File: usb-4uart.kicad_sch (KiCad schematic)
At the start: 49 parts, among them J1 Conn_02x05_Odd_Even, X1 24MHz

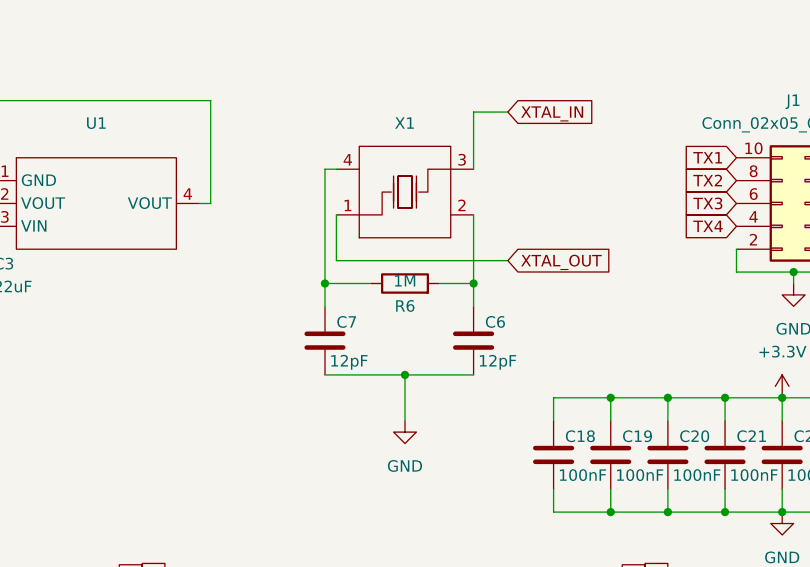
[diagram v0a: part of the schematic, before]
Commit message: -updated layout and traces -relocated caps -rotated devices -usb paths more even now
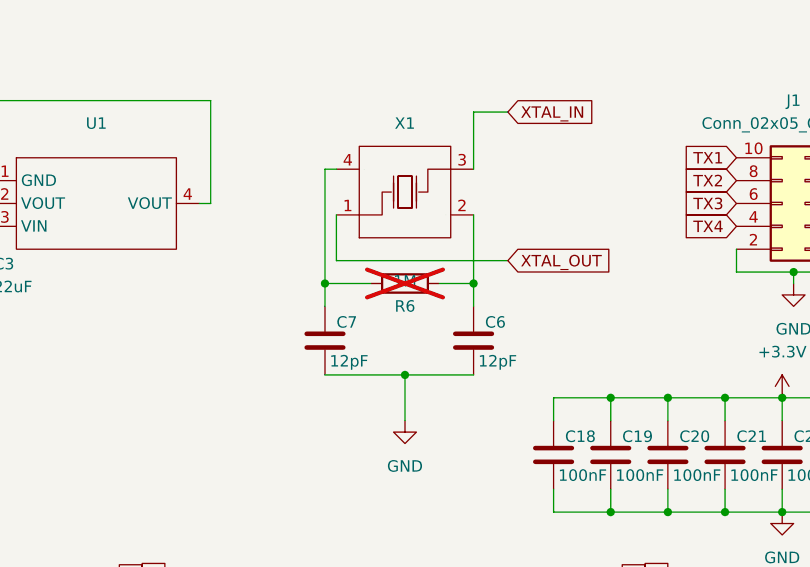
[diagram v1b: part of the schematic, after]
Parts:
- R6: now not fitted

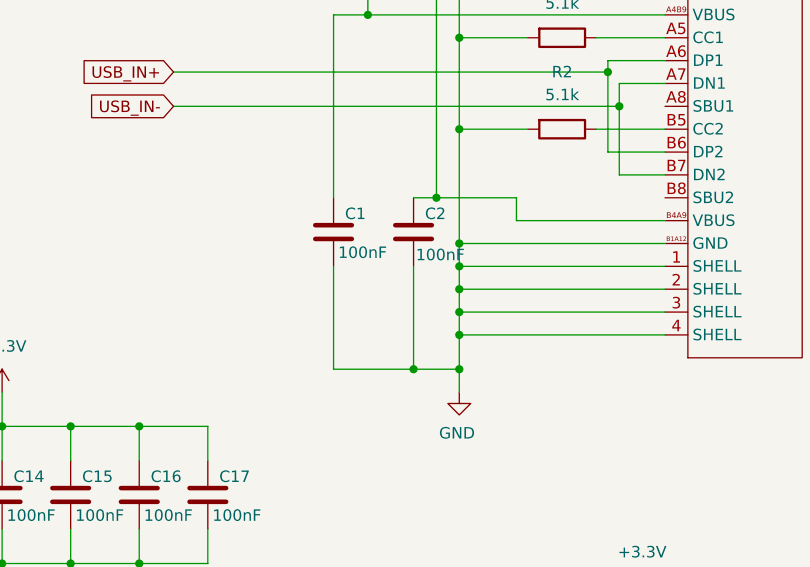
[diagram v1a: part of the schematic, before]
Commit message: updated cp2102 vias updated crystal circuitry updated 3v3 joints
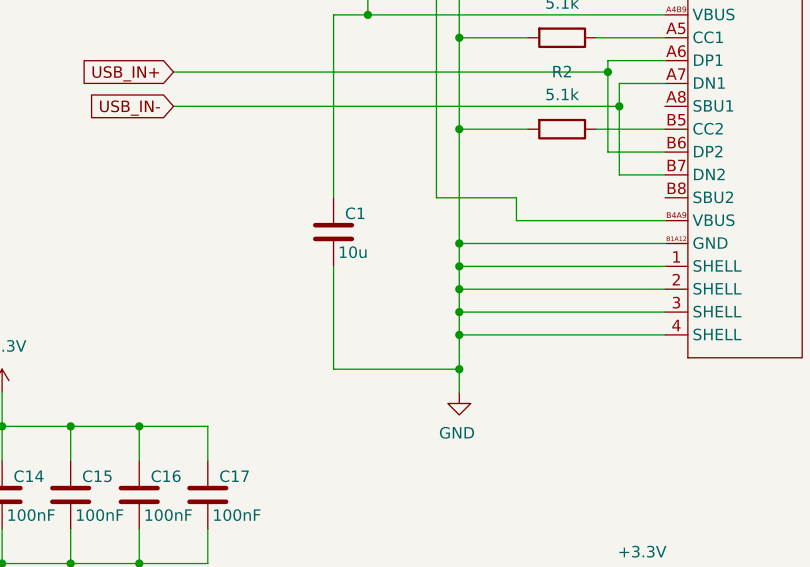
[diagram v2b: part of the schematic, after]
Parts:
- removed C2: 100nF, Capacitor_SMD:C_0201_0603Metric, symbol Device:C
- C1: value 100nF -> 10u
- C3: footprint Capacitor_Tantalum_SMD:CP_EIA-1608-08_AVX-J -> Capacitor_Tantalum_SMD:CP_EIA-3216-18_Kemet-A

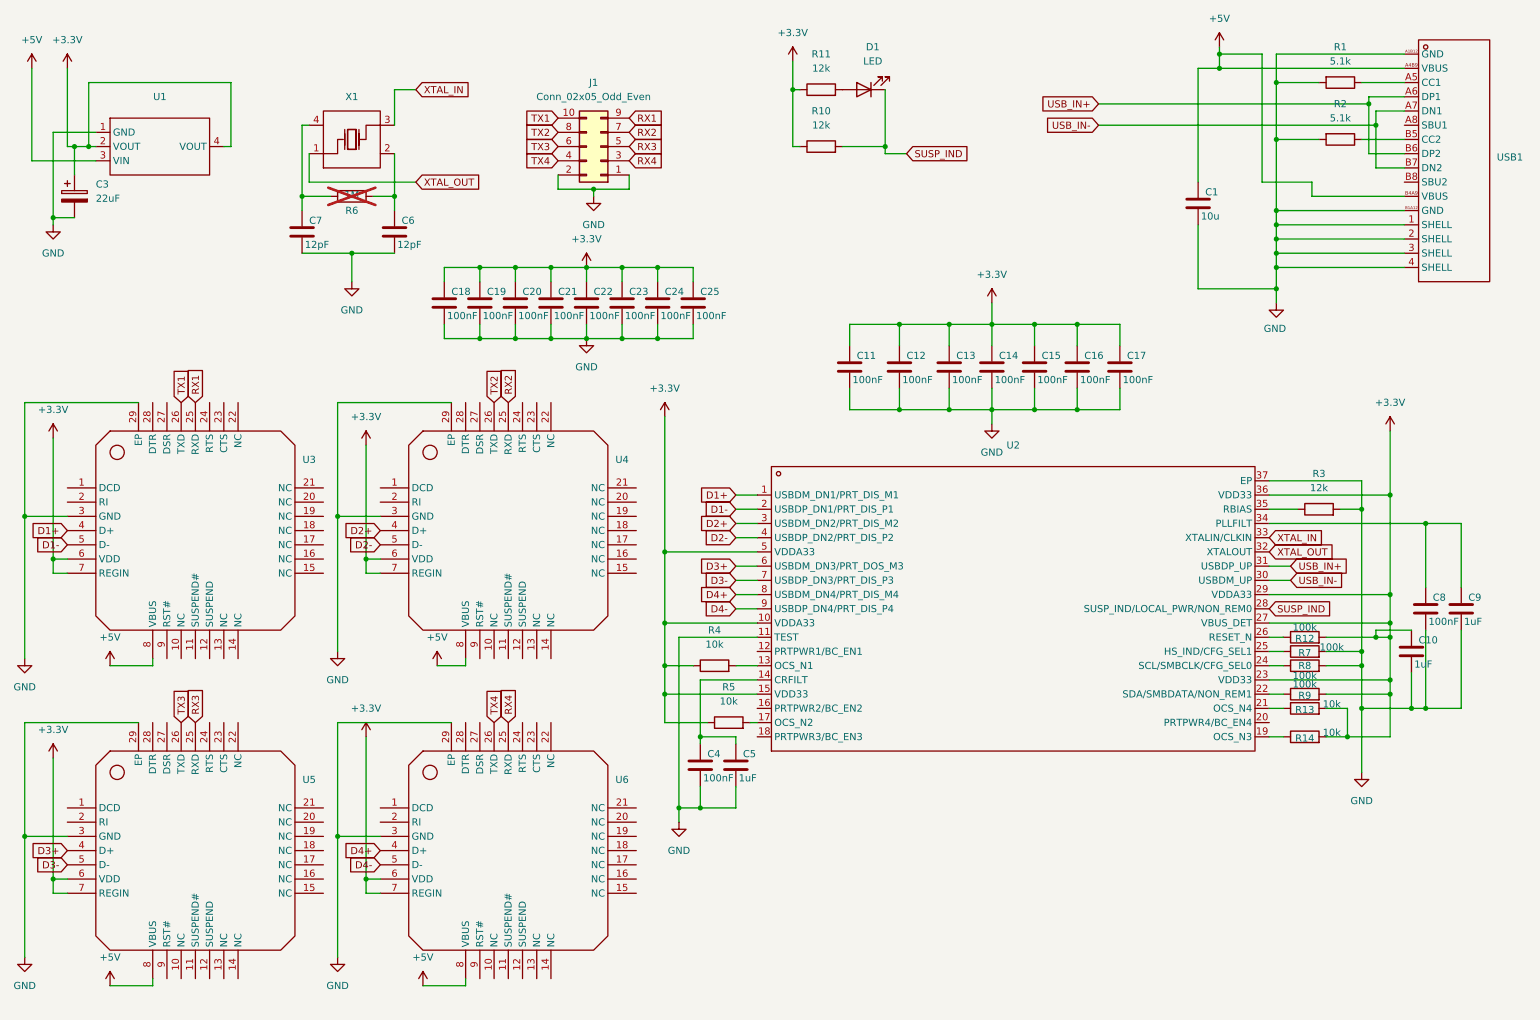
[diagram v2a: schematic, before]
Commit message: -updated to kicad 9.0.1 -reworked layout with correct footprints
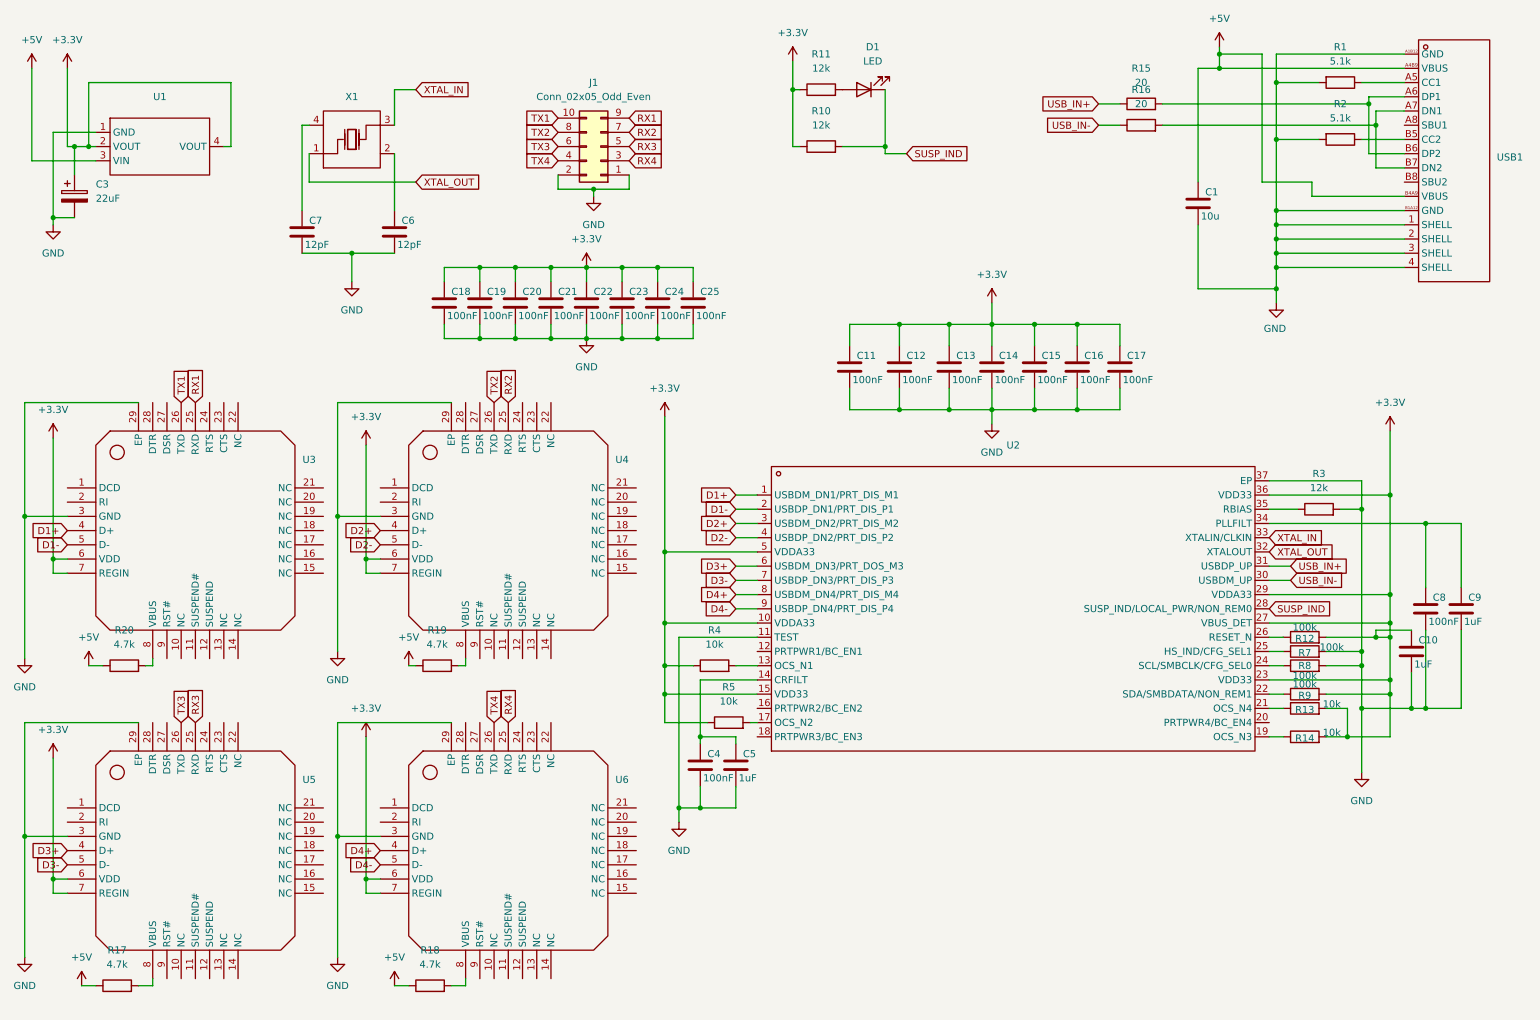
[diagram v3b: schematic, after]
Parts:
- removed R6: 1M, Resistor_SMD:R_0201_0603Metric, symbol Device:R
- added R15, R16: 20, Resistor_SMD:R_0402_1005Metric, symbol Device:R
- added R17, R18, R19, R20: 4.7k, Resistor_SMD:R_0402_1005Metric, symbol Device:R
- C10, C11, C12, C13, C14, C15, C16, C17, C18, C19, C20, C21, C22, C23, C24, C25, C4, C5, C6, C7, C8, C9: footprint Capacitor_SMD:C_0201_0603Metric -> Capacitor_SMD:C_0402_1005Metric
- R1, R10, R11, R12, R13, R14, R2, R3, R4, R5, R7, R8, R9: footprint Resistor_SMD:R_0201_0603Metric -> Resistor_SMD:R_0402_1005Metric
- U1: LCSC (none) -> C6186
- U2: LCSC (none) -> C16251
- U3, U4, U5, U6: LCSC (none) -> C6568
- USB1: LCSC (none) -> C393939
- X1: LCSC (none) -> C70590
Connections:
- net +5V: now also R17.1, R18.1, R19.1, R20.1; no longer U3.8 (VBUS), U4.8 (VBUS), U5.8 (VBUS), U6.8 (VBUS)
- net USB_IN+: now also R15.1; no longer USB1.A6 (DP1), USB1.B6 (DP2)
- net USB_IN-: now also R16.1; no longer USB1.A7 (DN1), USB1.B7 (DN2)
- new net: R15.2, USB1.A6 (DP1), USB1.B6 (DP2)
- new net: R16.2, USB1.A7 (DN1), USB1.B7 (DN2)
- new net: R19.2, U4.8 (VBUS)
- new net: R18.2, U6.8 (VBUS)
- new net: R20.2, U3.8 (VBUS)
- new net: R17.2, U5.8 (VBUS)
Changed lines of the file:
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@@
 (kicad_sch
-	(version 20231120)
+	(version 20250114)
 	(generator "eeschema")
-	(generator_version "8.0")
+	(generator_version "9.0")
 	(paper "A4")

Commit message: updated bom and clock
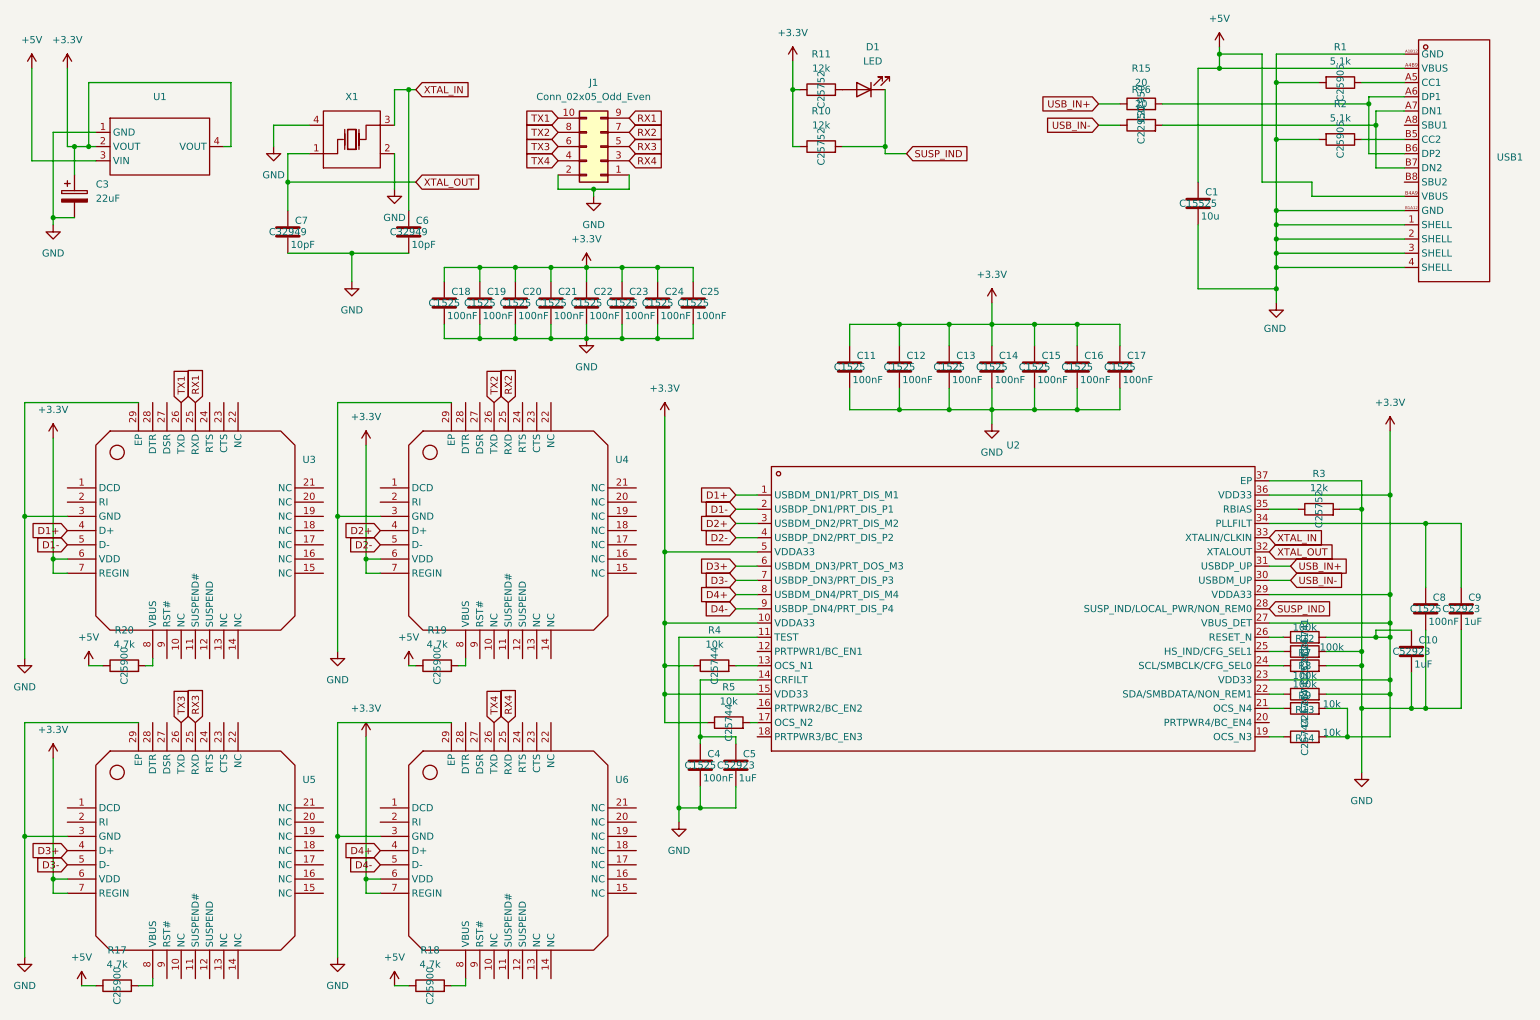
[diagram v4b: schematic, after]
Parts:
- C1: footprint Capacitor_SMD:C_0201_0603Metric -> Capacitor_SMD:C_0603_1608Metric; LCSC (none) -> C15525
- C10, C5, C9: LCSC (none) -> C52923
- C11, C12, C13, C14, C15, C16, C17, C18, C19, C20, C21, C22, C23, C24, C25, C4, C8: LCSC (none) -> C1525
- C6, C7: value 12pF -> 10pF; LCSC (none) -> C32949
- J1: LCSC C60563 -> C60563
- R1, R2: LCSC (none) -> C25905
- R10, R11, R3: LCSC (none) -> C25752
- R12, R7, R8, R9: LCSC (none) -> C25741
- R13, R14, R4, R5: LCSC (none) -> C25744
- R15, R16: footprint Resistor_SMD:R_0402_1005Metric -> Resistor_SMD:R_0603_1608Metric; LCSC (none) -> C22950
- R17, R18, R19, R20: LCSC (none) -> C25900
- X1: LCSC C70590 -> C70583; Supplier Part C70590 -> C70583
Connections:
- net GND: now also X1.2 (GND), X1.4 (GND)
- net XTAL_IN: now also C6.1
- net XTAL_OUT: now also C7.1
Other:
- moved on the sheet: C6, C7
